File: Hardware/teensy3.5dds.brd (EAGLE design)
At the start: 160 x 100 mm, 78 parts, among them IC1 AD8034ARZ, IC2 AD8034ARZ, IC3 AD8034ARZ, IC4 AD8034ARZ, IC5 AD8034ARZ, IC6 AD8034ARZ, IC7 AD8034ARZ, J1 1776275-2, J2 1776275-2, Q1 CSM-7X-DU, X1 1-227161-0

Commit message: hardware: better output select circuit And start arranging the components on the board
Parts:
- moved C1 464.5 mm to (29.2, 81.2), turned to 270 degrees
- moved X1 462.1 mm to (145.3, 2.29), turned to 180 degrees
- moved R9 461.8 mm to (33.0, 81.2), turned to 270 degrees
- moved C2 459.8 mm to (29.2, 77.3), turned to 270 degrees
- moved R2 458.4 mm to (38.1, 81.2), turned to 270 degrees
- moved J2 458.0 mm to (144.3, 93.0)
- moved C13 456.2 mm to (34.3, 77.3), turned to 270 degrees
- moved C3 455.1 mm to (29.2, 73.5), turned to 270 degrees
- moved R24 455.0 mm to (43.2, 81.2), turned to 270 degrees
- moved R3 452.0 mm to (38.1, 76.1), turned to 270 degrees
- moved C14 451.5 mm to (34.3, 73.5), turned to 270 degrees
- moved C4 450.5 mm to (29.2, 69.7), turned to 270 degrees
- moved R25 448.6 mm to (43.2, 76.1), turned to 270 degrees
- moved C15 446.9 mm to (34.3, 69.7), turned to 270 degrees
- moved IC6 446.1 mm to (49.5, 77.3), turned to 270 degrees
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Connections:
- new net N$37: R36.1, U$3.7, U$3.8, U$4.7, U$4.8
- net GND: no longer U$3.7, U$3.8, U$4.7, U$4.8
- net SQUARE_OUT: no longer R36.1
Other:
- board size 160 x 100 mm -> 160 x 101.3 mm

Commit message: hardware: switch to electronic opamp symbol * Add decoupling caps for each opamp IC * Change place to peak detector circuit, although the whole circuit needs to be changed
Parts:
- removed IC3, IC4, IC5, IC6, IC7: AD8034ARZ, AD8034ARZ:SOIC127P600X175-8N
- removed R12, R21, R22, R23, R24, R25, R26, R27, R28: (no value), rcl:M0805
- removed R13, R14, R32, R33, R34, R35, R37, R38: (no value), rcl:PT-10
- removed R36, R39, R40: (no value), rcl:R0805
- added C10, C11, C12, C21, C22, C23, C24, C25, C26, C27, C28, C29, C30, C31, C32, C33: (no value), rcl:C0805
- added IC10, IC11, IC12, IC8, IC9: AD8034, linear:SO08
- added R20, R29, R30, R31, R41, R42, R43, R44, R47, R48, R51, R52, R55, R56: (no value), rcl:R0805
- added R45, R46: (no value), rcl:PT-10
- added R49, R50, R53, R54, R57, R58: (no value), rcl:M0805
- C1, C13, C14, C15, C16, C17, C18, C19, C2, C20, C3, C4: device rcl:C0805K -> rcl:C0805
- IC1, IC2: value AD8034ARZ -> AD8034; device AD8034ARZ:SOIC127P600X175-8N -> linear:SO08
- R1, R10, R11, R4, R5, R6, R7, R8, R9: device rcl:M0805 -> rcl:R0805
- R2, R3: device rcl:M0805 -> rcl:PT-10
- moved R9 577.8 mm to (-61.0, -488.9), turned to 0 degrees
- moved R10 574.5 mm to (-61.0, -494.0), turned to 0 degrees
- moved R11 564.6 mm to (-61.0, -499.1), turned to 0 degrees
- moved R4 543.6 mm to (-61.0, -463.6), turned to 0 degrees
- moved R5 543.6 mm to (-61.0, -468.6), turned to 0 degrees
- moved R6 543.6 mm to (-61.0, -473.7), turned to 0 degrees
- moved R7 543.6 mm to (-61.0, -478.8), turned to 0 degrees
- moved R8 543.6 mm to (-61.0, -483.9), turned to 0 degrees
- moved IC1 528.3 mm to (-26.7, -429.3), turned to 0 degrees
- moved R2 518.7 mm to (-47.0, -430.5), turned to 0 degrees
- moved R3 515.7 mm to (-58.4, -430.5), turned to 0 degrees
- moved IC2 515.0 mm to (-36.8, -429.3), turned to 0 degrees
- moved R1 495.5 mm to (-38.1, -438.1), turned to 0 degrees
- moved C20 476.4 mm to (-17.8, -422.9), turned to 0 degrees
- moved C19 475.2 mm to (-17.8, -417.8), turned to 0 degrees
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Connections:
- removed net N$12: R13.3, R7.1
- removed net N$17: C4.1, R11.2, R12.1
- removed net N$18: C13.1, IC3.3, R22.2
- removed net N$19: C14.2, IC3.1, IC3.2, R23.1
- removed net N$2: IC1.1, IC1.2, R1.1
- removed net N$20: C14.1, R21.2, R22.1
- removed net N$21: C16.2, IC3.6, IC3.7, R27.1
- removed net N$23: C16.1, R23.2, R24.1
- removed net N$24: C17.1, IC4.3, R26.2
- removed net N$26: C18.1, R25.2, R26.1
- removed net N$27: S1.2
- removed net N$28: C19.2, IC4.5, R28.2
- removed net N$29: C20.1, R27.2, R28.1
- removed net N$37: R36.1, U$3.7, U$3.8, U$4.7, U$4.8
- removed net N$43: IC5.2, R35.1, R36.2
- removed net N$44: IC5.1, IC5.5, R35.3
- removed net N$45: IC5.3, R34.3, R37.2
- removed net N$46: IC7.2, R37.3, R39.1
- removed net N$47: D1.A, IC5.6, IC5.7, X1.1
- removed net N$48: IC7.5, R33.3
- removed net N$49: IC7.3, R32.3
- removed net N$52: C9.1, D1.C, R38.2
- removed net N$55: IC7.7, R40.1
- removed net N$7: IC1.5, R3.2, R4.2
- new net N$38: IC9.1, IC9.2, R30.2
- new net N$41: IC8.1, IC8.2, R43.2
- new net N$50: C11.2, R47.2, R48.1
- new net N$51: IC8.6, R43.1, R44.2
- new net N$53: C11.1, IC10.1, IC10.2, R49.1
- new net N$54: IC8.5, R41.2, R42.2
- new net N$56: R41.1, R45.3
- new net N$57: IC9.6, R30.1, R31.2
- new net N$58: C10.2, IC10.3, R48.2
- new net N$59: IC9.5, R20.2, R29.2
- new net N$60: R20.1, R46.3
- new net N$61: C21.1, R49.2, R50.1
- new net N$62: C21.2, IC10.6, IC10.7, R55.1
- new net N$63: C12.2, IC10.5, R50.2
- new net N$66: C23.2, R51.2, R52.1
- new net N$67: C23.1, IC11.1, IC11.2, R53.1
- new net N$68: C22.2, IC11.3, R52.2
- new net N$69: C25.1, R53.2, R54.1
- new net N$70: C25.2, IC11.6, IC11.7, R57.1
- new net N$71: C24.2, IC11.5, R54.2
- new net N$73: C27.2, R55.2, R56.1
- new net N$75: C26.2, IC12.3, R56.2
- new net N$76: C29.1, R57.2, R58.1
- new net N$78: C28.2, IC12.5, R58.2
- new net V*: R8.1
- net AMPL_MEASURE: now also IC2.7, R11.2; no longer IC7.6, R38.3, R40.2
- net DAC0: now also IC8.3; no longer IC1.3
- net DAC0_FILTERED: now also C27.1, IC12.1, IC12.2; no longer C20.2, IC4.6, IC4.7
- net DAC0_OFFSET: now also IC8.7, R44.1, R47.1; no longer IC1.7, R2.2, R21.1
- net GND: now also C10.1, C12.1, C14.2, C15.2, C16.1, C17.1, C18.1, C2.2, C20.1, C22.1, C24.1, C26.1, C28.1, C3.2, C30.1, C31.1, C33.1, C4.2, R29.1, R42.1, S1.2; no longer C15.1, C17.2, C3.1, R4.1, R8.1
- net N$10: now also R1.1; no longer IC2.6, R5.2, R6.1
- net N$11: now also IC2.2, R6.2, R7.2; no longer C1.1, IC6.3, R10.2
- net N$13: now also IC2.3, R4.1, R5.2; no longer IC2.5, R7.2, R8.2
- net N$14: now also C32.2, D1.C; no longer C2.2, IC6.1, IC6.2, R11.1
- net N$15: now also C32.1, R10.2; no longer C4.2, IC6.6, IC6.7, R25.1
- net N$16: now also IC2.6, R10.1, R11.1; no longer C3.2, IC6.5, R12.2
- net N$22: now also IC2.5, R8.2, R9.1; no longer C15.2, IC3.5, R24.2
- net N$3: now also IC1.3, R3.3, R6.1; no longer IC1.6, R1.2, R2.1
- net N$5: now also IC1.2, R1.2, R2.2; no longer C2.1, R10.1, R9.2
- net N$6: now also IC1.6, IC1.7, X1.1; no longer R14.3, R3.1
- net N$9: now also D1.A, IC1.1, IC1.5, R2.1, R2.3; no longer IC2.1, IC2.2, R5.1
- net OFF_MEASURE: now also IC2.1, R7.1; no longer IC7.1, R39.2
- net SQUARE: now also IC9.3; no longer IC2.3
- net SQUARE_FILTERED: now also C29.2, IC12.6, IC12.7; no longer C18.2, IC4.1, IC4.2
- net SQUARE_OFFSET: now also IC9.7, R31.1, R51.1; no longer IC2.7, R6.2, R9.1
- net V+: now also C1.1, C13.1, C14.1, C15.1, C2.1, C3.1, C4.1, C9.1, IC10.8, IC11.8, IC12.8, IC8.8, IC9.8, R3.2, R4.2, R45.2, R46.2; no longer IC3.8, IC4.8, IC5.8, IC6.8, IC7.8, R13.1, R14.1, R32.2, R33.2, R34.2
- net V-: now also C16.2, C17.2, C18.2, C19.2, C20.2, C30.2, C31.2, C33.2, IC10.4, IC11.4, IC12.4, IC8.4, IC9.4, R3.1, R45.1, R46.1, R5.1, R9.2; no longer IC3.4, IC4.4, IC6.4, IC7.4, R13.2, R14.2, R32.1, R33.1, R34.1

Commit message: hardware: add interrupt pin between 32u4 and teensy
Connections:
- new net INTERRUPT: U$1.37/A18, U$2.25
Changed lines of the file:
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@@
 <wire x1="-61.91" y1="-488.95" x2="-60.01" y2="-483.87" width="0" layer="19" extent="1-1"/>
+</signal>
+<signal name="INTERRUPT">
+<contactref element="U$2" pad="25"/>
+<contactref element="U$1" pad="37/A18"/>
+<wire x1="14.211" y1="26.755" x2="22.86" y2="45.72" width="0" layer="19" extent="1-1"/>
 </signal>
 </signals>

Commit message: hardware: better relay switching circuit
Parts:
- removed R18, R19: (no value), rcl:R0805
- added D2, D3: (no value), diode:SOD323-W
- added R12, R13: (no value), rcl:M0805
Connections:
- removed net N$15: C32.1, R10.2
- removed net N$33: C7.2, C8.-, LED_ON.C, RESET.P$1
- removed net N$34: Q3.2, R19.1
- removed net N$36: Q2.2, R18.1
- removed net N$39: Q2.3, U$3.13
- removed net N$40: Q3.3, U$4.13
- new net N$12: D2.A, Q3.2, U$4.6
- new net N$2: D3.A, Q2.2, U$3.6
- net +5V: no longer R18.2, R19.2
- net DAC0_SEL: now also R13.1, R13.2
- net GND: now also C32.1, C7.2, C8.-, LED_ON.C, Q2.3, Q3.3, RESET.P$1; no longer U$3.6, U$4.6
- net N$10: now also U$3.7, U$3.8, U$4.7, U$4.8
- net N$14: now also R10.2
- net SQUARE_SEL: now also R12.1, R12.2
- net V+: now also D2.C, D3.C, U$3.13, U$4.13

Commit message: hardware: switch to AD737 instead of peak detector circuit Peak detector needed external impedance decoupling and would not have worked when the offset was different from 0 or when the amplification lead the OpAmps into saturation AD737 is a True-RMS-to-DC converter, which works perfectly for this situation, coming at just 1$ more than an AD8034 IC
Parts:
- removed C32: (no value), rcl:C0805
- removed D1: (no value), diode:SOD323-W
- added IC3: AD8034, linear:SO08
- added IC4: AD737KRZ-R7, AD737KRZ-R7:SOIC127P600X175-8N
- moved R13 738.3 mm to (369.8, 70.0), turned to 90 degrees
- moved R12 731.2 mm to (364.7, 70.0), turned to 90 degrees
- moved D3 724.1 mm to (359.7, 70.0), turned to 90 degrees
- moved D2 717.0 mm to (354.6, 70.0), turned to 90 degrees
- moved C33 709.9 mm to (349.5, 70.0), turned to 90 degrees
- moved C9 702.9 mm to (344.4, 70.0), turned to 90 degrees
- moved R7 667.5 mm to (319.0, 70.0), turned to 90 degrees
- moved R6 660.4 mm to (313.9, 70.0), turned to 90 degrees
- moved R5 653.4 mm to (308.9, 70.0), turned to 90 degrees
- moved R4 646.3 mm to (303.8, 70.0), turned to 90 degrees
- moved C31 618.9 mm to (273.3, 113.2), turned to 90 degrees
- moved R1 618.1 mm to (278.4, 92.8), turned to 90 degrees
- moved C30 612.1 mm to (268.2, 113.2), turned to 90 degrees
- moved IC1 610.2 mm to (269.5, 104.3), turned to 90 degrees
- moved IC2 606.4 mm to (269.5, 94.1), turned to 90 degrees
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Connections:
- net AMPL_MEASURE: now also IC3.7; no longer IC2.7
- net GND: now also IC4.3, IC4.8; no longer C32.1
- net N$14: now also IC4.6, R10.1; no longer C32.2, D1.C, R10.2
- net N$16: now also IC3.6, R10.2; no longer IC2.6, R10.1
- net N$22: now also IC3.5; no longer IC2.5
- net N$9: now also IC4.2; no longer D1.A
- net V+: now also IC3.8, IC4.7
- net V-: now also IC3.4, IC4.4, IC4.5

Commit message: hardware: start arranging components on the board
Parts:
- removed IC3: AD8034, linear:SO08
- removed R2, R3, R45, R46: (no value), rcl:PT-10
- added R14, R18: (no value), rcl:RTRIM3296W
- added R19: (no value), rcl:R0805
- added R26, R27: POTENTIOMETER_VERTICAL, Potentiometer_vertical:MA03-1
- LED_ON: device adafruit:CHIP-LED0603 -> led:CHIPLED_1206
- moved C33 328.1 mm to (26.2, 14.4), turned to 0 degrees
- moved C9 307.4 mm to (41.4, 18.2), turned to 0 degrees
- moved R4 292.5 mm to (14.9, 24.3)
- moved R6 292.5 mm to (25.0, 24.3)
- moved R7 292.5 mm to (30.1, 24.3)
- moved R5 292.5 mm to (19.9, 24.3)
- moved R12 288.9 mm to (77.7, 37.0)
- moved R1 278.5 mm to (8.51, 24.3)
- moved D3 269.9 mm to (91.3, 40.9), turned to 180 degrees
- moved R13 265.9 mm to (105.7, 39.5)
- moved C31 251.1 mm to (33.8, 37.8), turned to 0 degrees
- moved D2 235.8 mm to (120.8, 39.1), turned to 0 degrees
- moved IC2 235.4 mm to (40.3, 40.8)
- moved C30 234.5 mm to (54.1, 17.5), turned to 0 degrees
- moved IC1 223.9 mm to (61.8, 20.4)
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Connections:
- removed net V*: R8.1
- new net N$15: R19.2, R26.2
- net AMPL_MEASURE: now also IC2.7; no longer IC3.7
- net N$16: now also IC2.5; no longer IC3.6
- net N$22: now also IC2.6; no longer IC3.5
- net N$3: now also R27.3; no longer R3.3
- net N$5: now also R19.1; no longer R2.2
- net N$56: now also R18.2; no longer R45.3
- net N$60: now also R14.2; no longer R46.3
- net N$9: now also R26.1, R26.3; no longer R2.1, R2.3
- net V+: now also R14.3, R18.3, R27.2, R8.1; no longer IC3.8, R3.2, R45.2, R46.2
- net V-: now also R14.1, R18.1, R27.1; no longer IC3.4, R3.1, R45.1, R46.1

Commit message: hardware: board v0.1
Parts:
- removed R26, R27: POTENTIOMETER_VERTICAL, Potentiometer_vertical:MA03-1
- added U$5, U$6: POTENTIOMETER_VERTICAL, Potentiometer_vertical:MA03-1
- moved J1 106.7 mm to (113.7, 86.0), turned to 90 degrees
- moved J2 95.5 mm to (113.7, 74.3), turned to 90 degrees
- moved U$1 93.5 mm to (31.0, 89.2), turned to 0 degrees
- moved J_DISPLAY 70.3 mm to (27.8, 72.4)
- moved D2 64.0 mm to (57.4, 47.8)
- moved C26 51.1 mm to (93.5, 39.1), turned to 0 degrees
- moved C27 50.4 mm to (93.5, 44.1), turned to 180 degrees
- moved U$4 50.1 mm to (65.0, 34.5), turned to 270 degrees
- moved Q3 50.0 mm to (63.5, 53.7), turned to 0 degrees
- moved R13 49.7 mm to (57.5, 51.8), turned to 0 degrees
- moved J_OUT_DAC 49.4 mm to (73.0, 53.0), turned to 0 degrees
- moved R1 48.0 mm to (56.4, 26.9), turned to 180 degrees
- moved R55 47.3 mm to (88.1, 46.6), turned to 0 degrees
- moved R58 45.2 mm to (109.7, 37.7), turned to 180 degrees
- moved C13 45.0 mm to (104.6, 48.3), turned to 90 degrees
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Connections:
- removed net N$6: IC1.6, IC1.7, X1.1
- new net N$17: Q2.1, R12.2
- new net N$18: Q3.1, R13.2
- new net N$19: IC1.1, IC1.2, X1.1
- net DAC0_SEL: no longer Q3.1, R13.2
- net GND: no longer U$2.15, U$2.35, U$2.43, U$2.5
- net N$15: now also U$6.1; no longer R26.2
- net N$16: now also IC2.6; no longer IC2.5
- net N$22: now also IC2.5; no longer IC2.6
- net N$3: now also IC1.5, U$5.2; no longer IC1.3, R27.3
- net N$5: now also IC1.6; no longer IC1.2
- net N$67: now also R57.1; no longer R53.1
- net N$70: now also R51.1; no longer R57.1
- net N$9: now also IC1.3, IC1.7, U$6.2, U$6.3; no longer IC1.1, IC1.5, R26.1, R26.3
- net RX1: now also U$1.32/A13; no longer U$1.33/A14
- net SQUARE_OFFSET: now also R53.1; no longer R51.1
- net SQUARE_SEL: no longer Q2.1, R12.2
- net TX1: now also U$1.31/A12; no longer U$1.34/A15
- net V+: now also U$5.3; no longer R27.2
- net V-: now also U$5.1; no longer R27.1
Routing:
- net GND: track 0.00 -> 708.8 mm, vias 0 -> 18
- net +5V: track 0.00 -> 292.4 mm, vias 0 -> 1
- net SQUARE_SEL: track 0.00 -> 138.6 mm, vias 0 -> 1
- net N$3: track 0.00 -> 92.5 mm, vias 0 -> 2
- net V-: track 0.00 -> 90.7 mm, vias 0 -> 8
- net INTERRUPT: track 0.00 -> 83.0 mm, vias 0 -> 1
- net N$19: track 0.00 -> 77.9 mm, vias 0 -> 1
- net DAC0_OFFSET: track 0.00 -> 77.7 mm, vias 0 -> 2
- net N$9: track 0.00 -> 73.3 mm, vias 0 -> 2
- net SQUARE_OFFSET: track 0.00 -> 67.3 mm, vias 0 -> 2
- net DAC0_SEL: track 0.00 -> 61.6 mm, vias 0 -> 1
- net SQUARE: track 0.00 -> 61.2 mm
- net N$8: track 0.00 -> 59.8 mm, vias 0 -> 1
- net N$25: track 0.00 -> 58.4 mm, vias 0 -> 1
- net N$1: track 0.00 -> 57.9 mm, vias 0 -> 1
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- added copper zone on layer 1, net V+
- added copper zone on layer 16, net V-
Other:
- board size 160 x 101.3 mm -> 118.4 x 90.9 mm

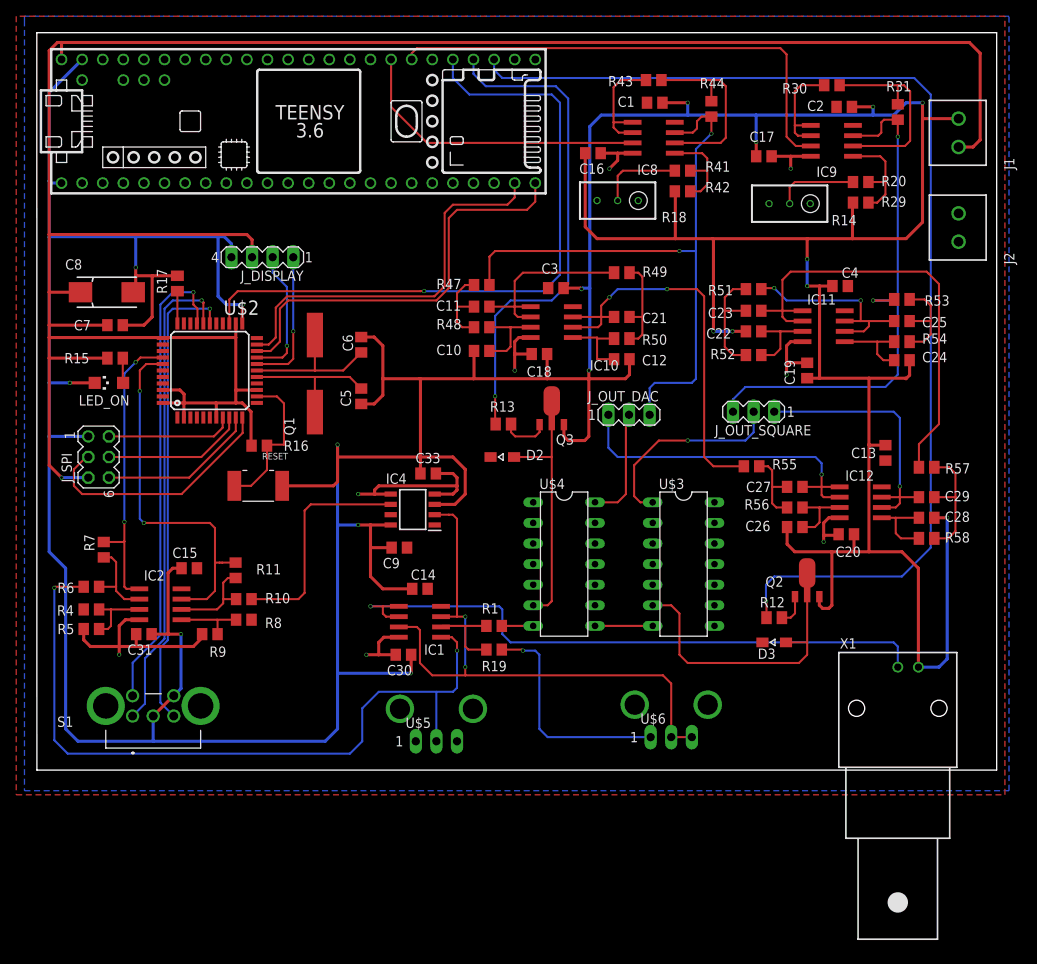
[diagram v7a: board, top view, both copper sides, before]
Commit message: hardware: board v0.2 shrink by 1cm on one side
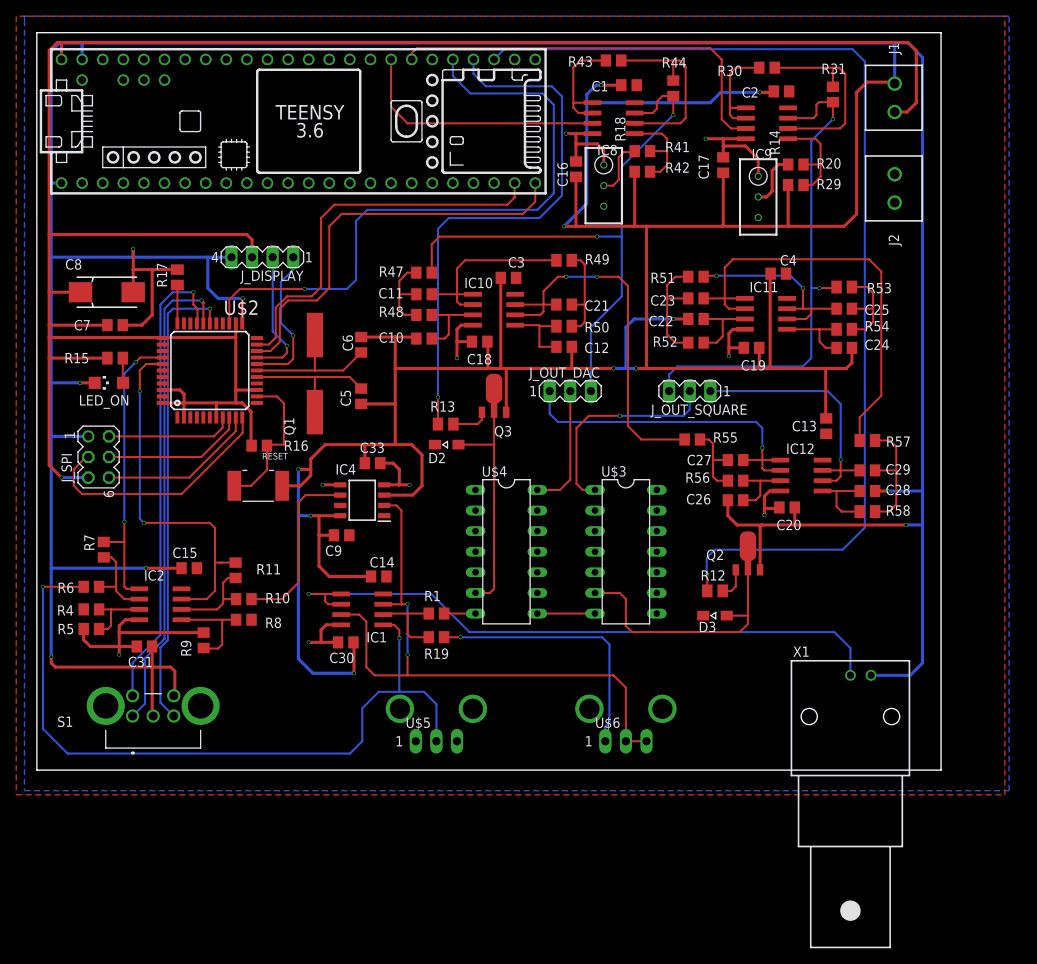
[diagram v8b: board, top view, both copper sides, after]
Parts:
- moved J2 9.24 mm to (105.8, 79.1)
- moved J1 8.98 mm to (105.8, 90.3)
- moved IC9 8.29 mm to (90.0, 88.9)
- moved R29 8.29 mm to (93.6, 81.3)
- moved R31 8.29 mm to (98.2, 92.5)
- moved R20 8.29 mm to (93.6, 83.8)
- moved R30 8.29 mm to (90.0, 95.8)
- moved J_OUT_SQUARE 8.27 mm to (80.5, 55.9)
- moved C20 8.01 mm to (92.5, 41.5)
- moved D3 8.01 mm to (83.6, 28.2)
- moved R12 8.01 mm to (83.6, 31.2)
- moved R55 8.01 mm to (80.8, 49.9)
- moved C13 8.01 mm to (97.3, 51.6)
- moved C26 8.01 mm to (86.2, 42.4)
- moved C27 8.01 mm to (86.2, 47.4)
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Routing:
- net GND: track 708.8 -> 796.0 mm, vias 18 -> 16
- net +5V: track 292.4 -> 280.3 mm
- net SQUARE: track 61.2 -> 50.7 mm
- net SQUARE_SEL: track 138.6 -> 129.5 mm
- net DAC0: track 37.5 -> 31.5 mm
- net N$14: track 28.0 -> 22.1 mm
- net DAC0_SEL: track 61.6 -> 67.1 mm
- net N$15: track 28.2 -> 32.9 mm
- net SQUARE_OFFSET: track 67.3 -> 63.3 mm
- net N$22: track 8.54 -> 12.3 mm
- net N$9: track 73.3 -> 76.9 mm
- net DAC0_OFFSET: track 77.7 -> 74.1 mm
- net INTERRUPT: track 83.0 -> 79.5 mm
- net N$60: track 10.1 -> 6.83 mm
- net N$56: track 10.4 -> 7.21 mm
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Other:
- board size 118.4 x 90.9 mm -> 111.5 x 90.9 mm
